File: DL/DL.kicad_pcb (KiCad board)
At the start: 2 copper layers, 97.8 x 116.8 mm, 39 parts, among them IC1 MCP6V96UT-E_OT, IC2 SCD42-D-R2, IC3 TGS3870-B00, J3 SD_Card, J4 Conn_01x05_Male, J5 Conn_01x05_Male, J6 Conn_01x05_Male, J7 Conn_01x05_Male, Q1 BSS84, Q2 2N7002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

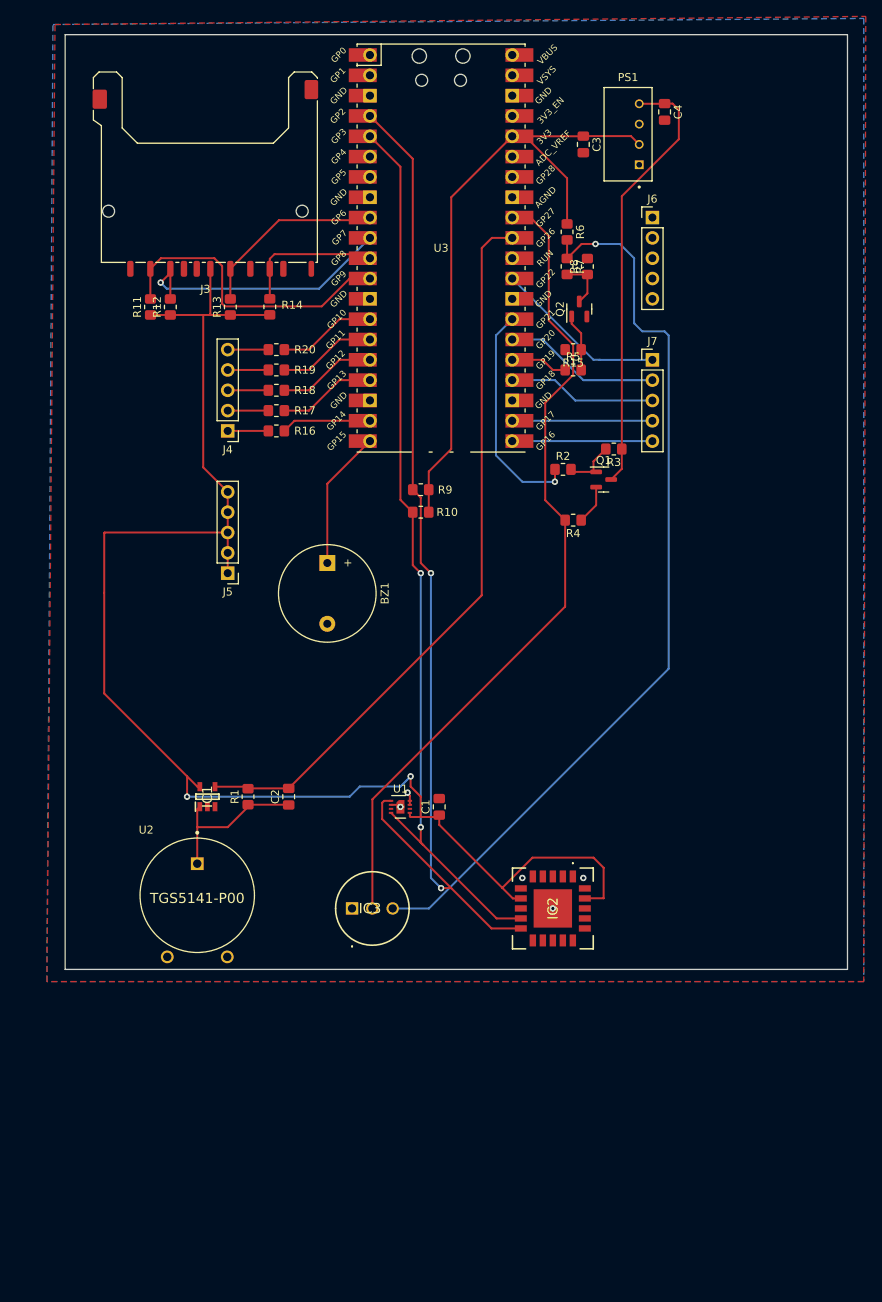
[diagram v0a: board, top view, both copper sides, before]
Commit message: Fixed edge cuts - Iteration no. 3
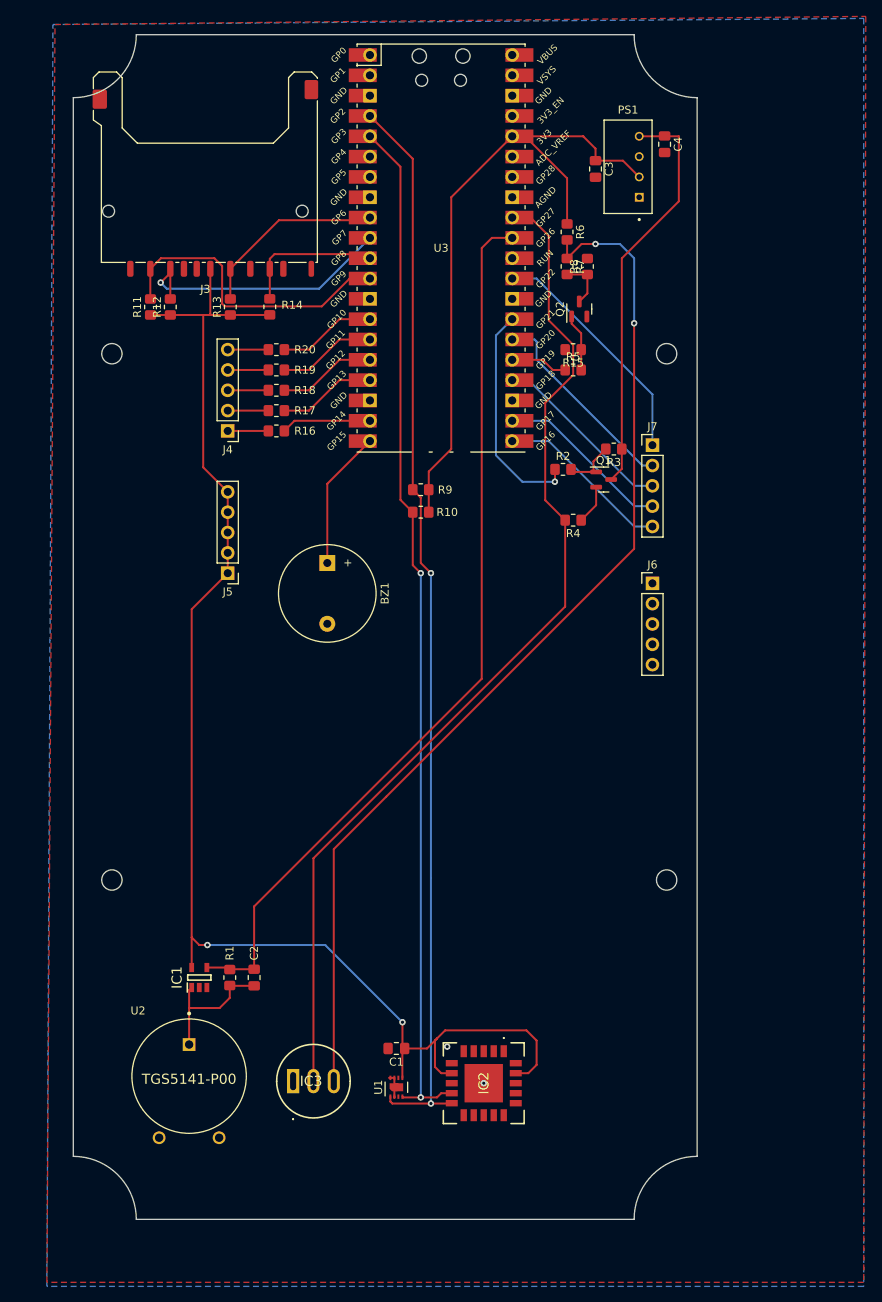
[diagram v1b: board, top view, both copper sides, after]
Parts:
- IC3: footprint TGS3870-B00:TGS3870B00 -> TGS3870B00:TGS3870B00
- moved J6 45.7 mm to (95.0, 86.4)
- moved U1 35.1 mm to (63.0, 149.4), turned to 90 degrees
- moved C1 30.7 mm to (63.0, 144.5), turned to 180 degrees
- moved IC2 23.5 mm to (73.9, 148.8)
- moved C2 23.0 mm to (45.2, 135.6)
- moved IC3 22.8 mm to (50.1, 148.6)
- moved R1 22.7 mm to (42.2, 135.6)
- moved U2 22.6 mm to (37.1, 148.3)
- moved IC1 22.6 mm to (38.4, 135.6)
- moved J7 10.7 mm to (95.0, 69.1)
- moved PS1 4.06 mm to (91.9, 34.3)
- moved C4 4.04 mm to (96.5, 31.5)
- moved C3 3.43 mm to (87.9, 34.6)
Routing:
- net GP27/ADC1/I2C_SCL1: track 103.3 -> 128.0 mm
- net GP26/ADC0/I2C_SDA1: track 91.2 -> 112.3 mm
- net VD: track 113.8 -> 130.6 mm, vias 1 -> 2
- net GP3/SPI_TX0/I2C_SCL1: track 113.0 -> 129.3 mm
- net GP22: track 21.7 -> 29.9 mm
- net +3.3V: track 266.5 -> 258.4 mm
- net GP2/SPI_SCK0/SDA1: track 127.7 -> 135.0 mm
- net GP20/I2C_SDA0: track 19.6 -> 25.4 mm
- net GP16/SPI_RX0/I2C_SDA0/UART_TX0: track 17.5 -> 22.0 mm
- net GP17/SPI_CSn0/I2C_SCL0/UART_RX0: track 17.5 -> 22.0 mm
- net GP18/SPI_SCK0/I2C_SDA1: track 18.6 -> 23.0 mm
- net +5V: track 55.0 -> 51.4 mm
- net Net-(C2-Pad1): track 20.0 -> 17.5 mm
- net AGND: track 3.05 -> 3.42 mm, vias 5 -> 2
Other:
- board size 97.8 x 116.8 mm -> 78 x 148.1 mm

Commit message: Git cynchro fixed
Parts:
- moved J6 51.2 mm to (86.9, 35.8)
- moved U1 35.1 mm to (63.5, 114.3), turned to 0 degrees
- moved C1 30.7 mm to (68.3, 114.3), turned to 90 degrees
- moved R16 23.6 mm to (42.1, 90.2)
- moved R17 23.6 mm to (42.1, 87.6)
- moved R19 23.6 mm to (42.1, 82.5)
- moved R18 23.6 mm to (42.1, 85.1)
- moved R20 23.6 mm to (42.1, 80.0)
- moved IC2 23.5 mm to (82.5, 127.0)
- moved J4 23.1 mm to (38.6, 90.2)
- moved J5 23.1 mm to (38.6, 107.9)
- moved C2 23.0 mm to (49.5, 113.0)
- moved IC3 22.8 mm to (57.5, 127.0)
- moved R1 22.7 mm to (44.5, 113.0)
- moved U2 22.6 mm to (38.1, 125.7)
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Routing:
- net +3.3V: track 258.4 -> 0.00 mm, vias 2 -> 0
- net GP2/SPI_SCK0/SDA1: track 135.0 -> 0.00 mm, vias 2 -> 0
- net VD: track 130.6 -> 0.00 mm, vias 2 -> 0
- net GP3/SPI_TX0/I2C_SCL1: track 129.3 -> 0.00 mm, vias 2 -> 0
- net GP27/ADC1/I2C_SCL1: track 128.0 -> 0.00 mm
- net GP26/ADC0/I2C_SDA1: track 112.3 -> 0.00 mm
- net +5V: track 51.4 -> 0.00 mm
- net GP9/SPI_CSn1/I2C_SCL0/UART_RX1: track 38.5 -> 0.00 mm
- net GP7/SPI_TX0/I2C_SCL1: track 35.1 -> 0.00 mm, vias 1 -> 0
- net GP22: track 29.9 -> 0.00 mm
- net GP21/I2C_SCL0: track 28.2 -> 0.00 mm, vias 1 -> 0
- net GP20/I2C_SDA0: track 25.4 -> 0.00 mm
- net GP6/SPI_SCK0/I2C_SDA1: track 23.9 -> 0.00 mm
- net GP18/SPI_SCK0/I2C_SDA1: track 23.0 -> 0.00 mm
- net GP16/SPI_RX0/I2C_SDA0/UART_TX0: track 22.0 -> 0.00 mm
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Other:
- board size 78 x 148.1 mm -> 79.8 x 149.9 mm

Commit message: Add files via upload
Added mounting holes, all items on edgeCuts layer are locked in place
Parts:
- moved J4 46.8 mm to (85.4, 87.6)
- moved J5 46.8 mm to (85.4, 105.4)
- moved R16 39.7 mm to (81.8, 87.6), turned to 180 degrees
- moved R17 39.7 mm to (81.8, 85.1), turned to 180 degrees
- moved R19 39.7 mm to (81.8, 80.0), turned to 180 degrees
- moved R20 39.7 mm to (81.8, 77.5), turned to 180 degrees
- moved R18 39.7 mm to (81.8, 82.5), turned to 180 degrees
- moved J3 26.1 mm to (31.0, 77.2), turned to 0 degrees
- moved R11 14.9 mm to (37.8, 61.3), turned to -90 degrees
- moved R14 12.6 mm to (25.4, 61.2), turned to -90 degrees
- moved R12 10.5 mm to (35.4, 61.3), turned to -90 degrees
- moved BZ1 9.35 mm to (57.9, 92.5)
- moved R13 8.51 mm to (27.9, 61.3), turned to -90 degrees
- moved J7 8.02 mm to (85.3, 61.5)
- moved J6 8.02 mm to (85.3, 43.7)
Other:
- outline, holes or cut-outs redrawn

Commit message: Final PCB design
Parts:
- added J1: Conn_01x02_Male, Connector_PinHeader_2.54mm:PinHeader_1x02_P2.54mm_Vertical, F.Cu at (70.4, 136.7)
- added J2: Conn_01x02_Male, Connector_PinHeader_2.54mm:PinHeader_1x02_P2.54mm_Vertical, F.Cu at (75.7, 136.7)
- IC3: footprint TGS3870B00:TGS3870B00 -> TGS3870-B00:TGS3870B00
- moved C1 25.7 mm to (58.2, 137.9)
- moved U1 25.7 mm to (53.3, 137.9)
- moved U2 25.5 mm to (35.8, 151.1)
- moved IC2 25.5 mm to (73.7, 150.9)
- moved C2 25.2 mm to (45.7, 137.9)
- moved R1 25.0 mm to (41.9, 137.9)
- moved IC1 25.0 mm to (36.8, 137.9)
- moved IC3 24.4 mm to (52.6, 150.9)
- moved BZ1 5.84 mm to (57.9, 86.6)
- moved J3 4.67 mm to (32.8, 81.5)
- moved R11 4.67 mm to (39.6, 65.6)
- moved R13 4.67 mm to (29.6, 65.6)
- moved R12 4.67 mm to (37.1, 65.6)
- moved R14 4.67 mm to (27.2, 65.6)
- moved R10 2.17 mm to (64.5, 79.0)
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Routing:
- net +3.3V: track 0.00 -> 304.7 mm, vias 0 -> 2
- net GP27/ADC1/I2C_SCL1: track 0.00 -> 166.9 mm, vias 0 -> 1
- net GP2/SPI_SCK0/SDA1: track 0.00 -> 164.7 mm, vias 0 -> 3
- net VD: track 0.00 -> 161.5 mm, vias 0 -> 2
- net GP3/SPI_TX0/I2C_SCL1: track 0.00 -> 155.9 mm, vias 0 -> 1
- net GP26/ADC0/I2C_SDA1: track 0.00 -> 120.4 mm, vias 0 -> 3
- net +5V: track 0.00 -> 51.6 mm
- net GP8/SPI_RX1/I2C_SDA0/UART_TX1: track 0.00 -> 42.2 mm
- net GP6/SPI_SCK0/I2C_SDA1: track 0.00 -> 41.8 mm, vias 0 -> 1
- net GP13/SPI_CSn1/I2C_SCL0/UART_RX0: track 0.00 -> 39.4 mm, vias 0 -> 1
- net GP11/SPI_TX1/I2C_SCL1: track 0.00 -> 39.4 mm, vias 0 -> 1
- net GP10/SPI_SCK1/I2C_SDA1: track 0.00 -> 39.4 mm, vias 0 -> 1
- net GP12/SPI_RX1/I2C_SDA0/UART_TX0: track 0.00 -> 39.4 mm, vias 0 -> 1
- net GP14/SPI_SCK1/I2C_SDA1: track 0.00 -> 38.4 mm, vias 0 -> 1
- net GP7/SPI_TX0/I2C_SCL1: track 0.00 -> 38.1 mm, vias 0 -> 1
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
